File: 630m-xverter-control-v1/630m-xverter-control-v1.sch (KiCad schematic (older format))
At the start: 52 parts, among them J1 Rig Transverter, J2 ALC, J3 ANT, J4 TX_TO_AMP, J5 TX_FROM_AMP, J6 Power, J7 TX AMP POWER, K1 DS1E-M-DC12V, K2 DS1E-M-DC12V, K3 DS1E-M-DC12V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

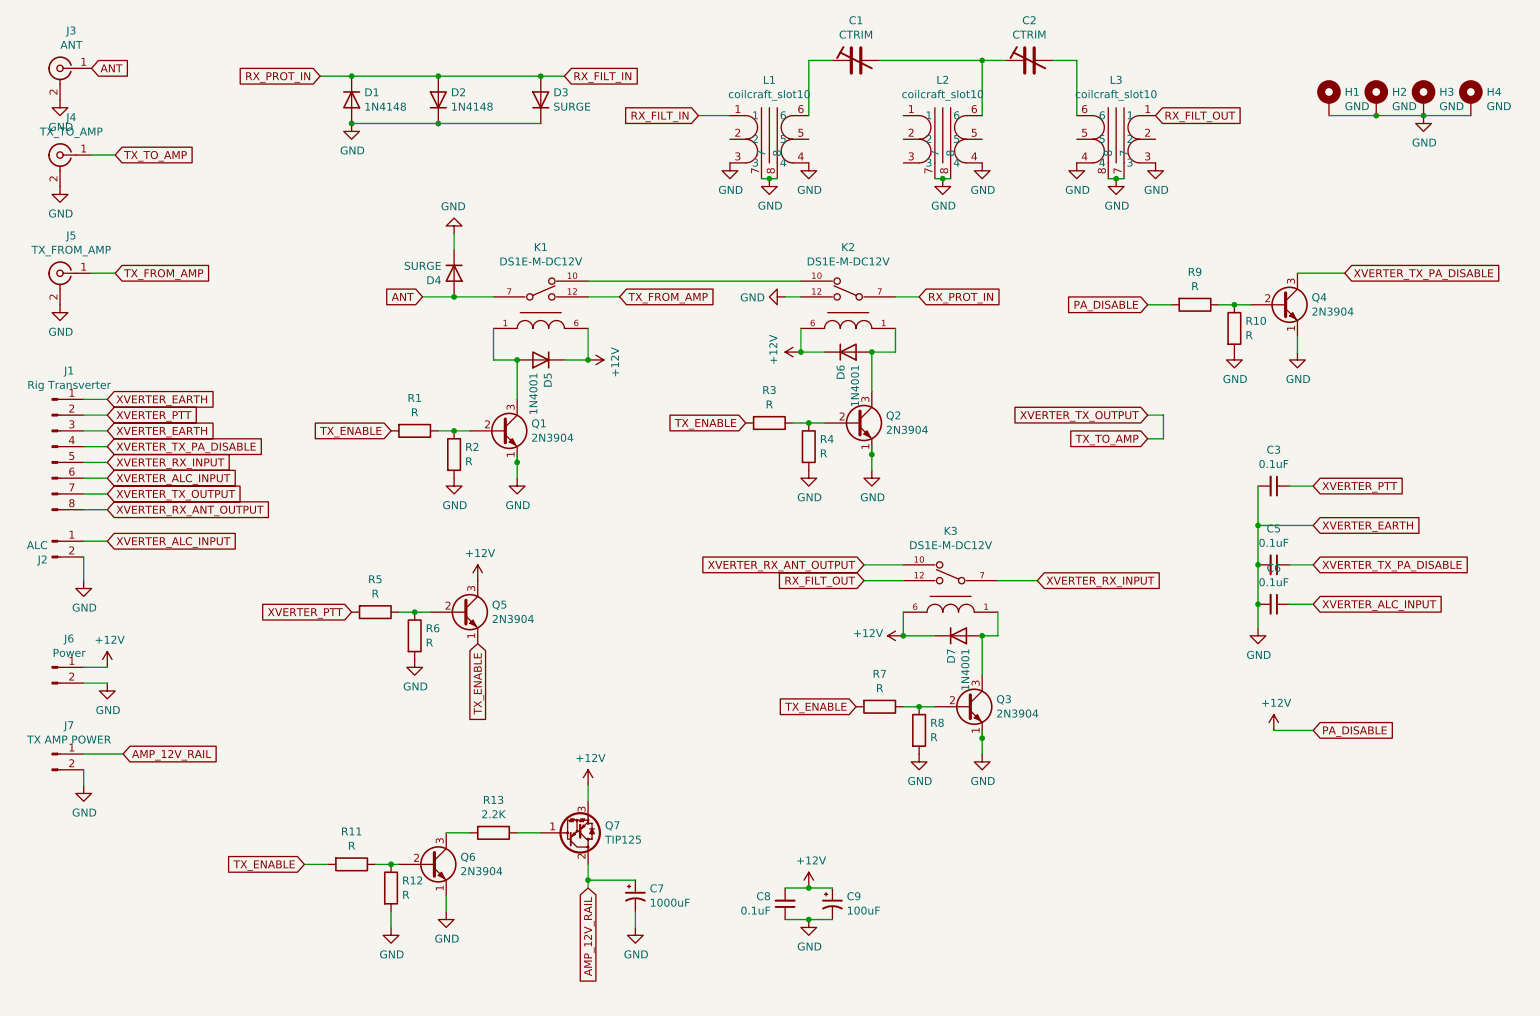
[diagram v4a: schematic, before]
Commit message: I got the fucking relay power backwards. WTAF.
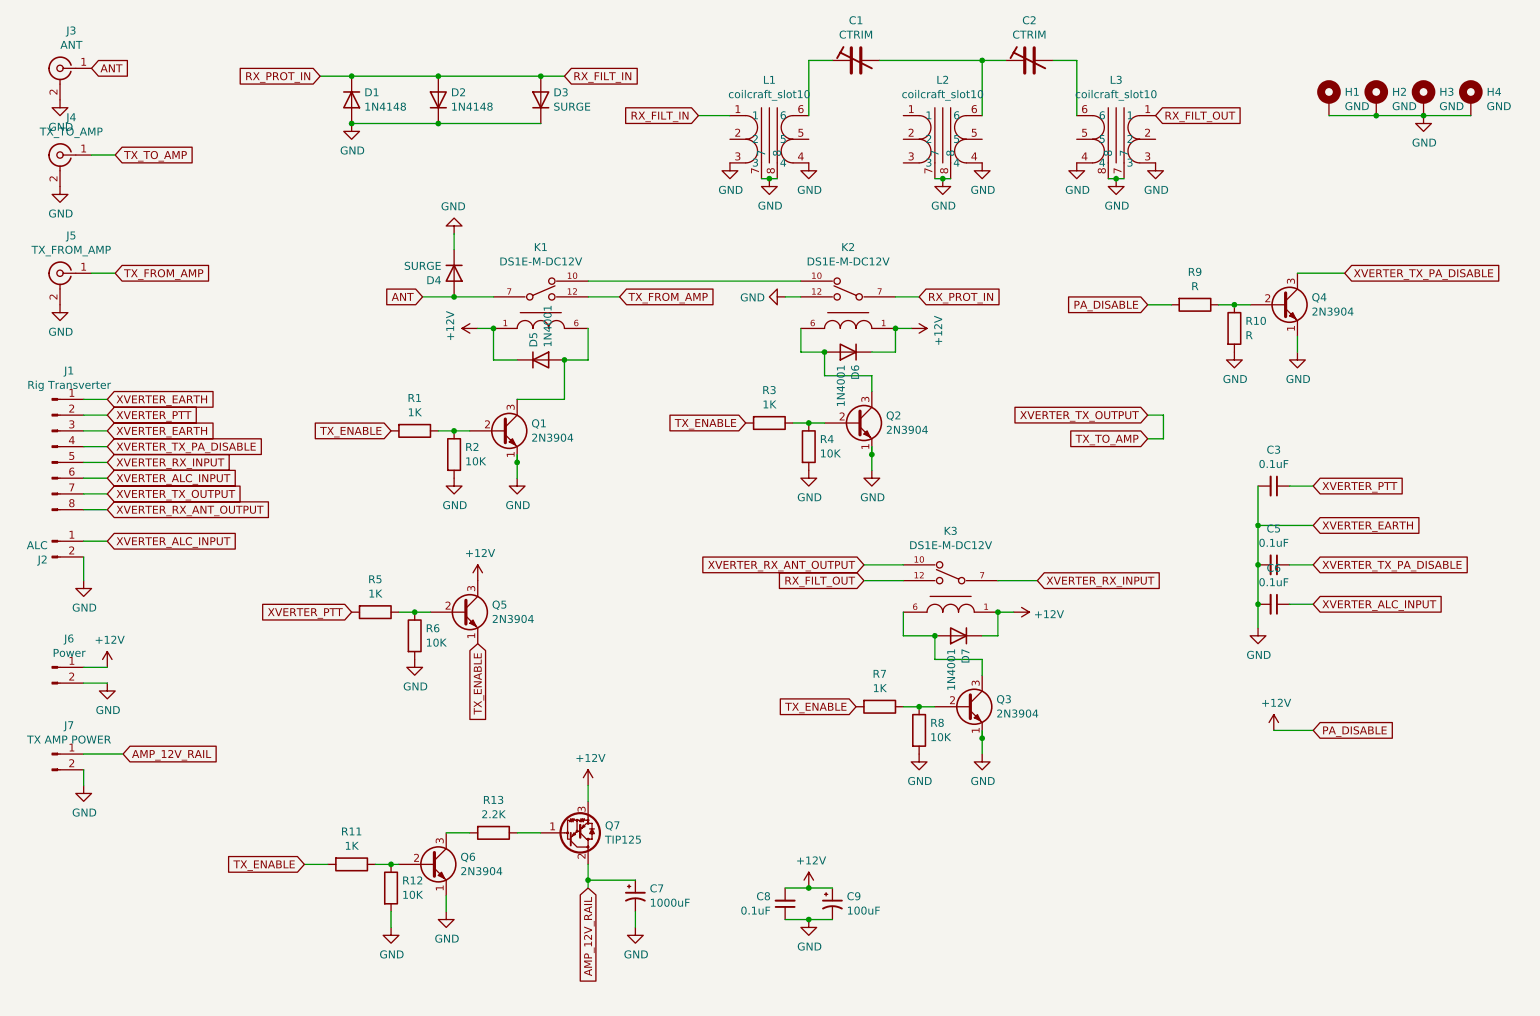
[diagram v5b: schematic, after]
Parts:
- C7: footprint Capacitor_THT:CP_Radial_D10.0mm_P2.50mm -> Capacitor_THT:CP_Radial_D10.0mm_P5.00mm
- R1, R11, R3, R5, R7: value R -> 1K
- R12, R2, R4, R6, R8: value R -> 10K
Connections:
- net +12V: now also K1.1, K2.1, K3.1; no longer K1.6, K2.6, K3.6
- net at D5.2 (A), Q1.3 (C): now also K1.6; no longer K1.1
- net at D6.2 (A), Q2.3 (C): now also K2.6; no longer K2.1
- net at D7.2 (A), Q3.3 (C): now also K3.6; no longer K3.1
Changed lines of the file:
@@
 P 3200 4300
 F 0 "R5" V 2993 4300 50  0000 C CNN
-F 1 "R" V 3084 4300 50  0000 C CNN
+F 1 "1K" V 3084 4300 50  0000 C CNN
 F 2 "Resistor_THT:R_Axial_DIN0207_L6.3mm_D2.5mm_P7.62mm_Horizontal" V 3130 4300 50  0001 C CNN
 F 3 "~" H 3200 4300 50  0001 C CNN
@@
 P 3450 4450
 F 0 "R6" H 3520 4496 50  0000 L CNN
-F 1 "R" H 3520 4405 50  0000 L CNN
+F 1 "10K" H 3520 4405 50  0000 L CNN
 F 2 "Resistor_THT:R_Axial_DIN0207_L6.3mm_D2.5mm_P7.62mm_Horizontal" V 3380 4450 50  0001 C CNN
 F 3 "~" H 3450 4450 50  0001 C CNN
@@
 F 3 "~" H 4250 2700 50  0001 C CNN
 	1    4250 2700
-	-1   0    0    1
+	1    0    0    -1
 $EndComp
 $Comp
@@
 F 3 "~" H 6200 2650 50  0001 C CNN
 	1    6200 2650
-	1    0    0    1
+	-1   0    0    1
 $EndComp
 $Comp
@@
 F 3 "~" H 6900 4450 50  0001 C CNN
 	1    6900 4450
-	1    0    0    1
+	-1   0    0    1
 $EndComp
 Text GLabel 9350 2150 2    50   Input ~ 0
@@
 P 3450 3150
 F 0 "R1" V 3243 3150 50  0000 C CNN
-F 1 "R" V 3334 3150 50  0000 C CNN
+F 1 "1K" V 3334 3150 50  0000 C CNN
 F 2 "Resistor_THT:R_Axial_DIN0207_L6.3mm_D2.5mm_P7.62mm_Horizontal" V 3380 3150 50  0001 C CNN
 F 3 "~" H 3450 3150 50  0001 C CNN
@@
 P 3700 3300
 F 0 "R2" H 3770 3346 50  0000 L CNN
-F 1 "R" H 3770 3255 50  0000 L CNN
+F 1 "10K" H 3770 3255 50  0000 L CNN
 F 2 "Resistor_THT:R_Axial_DIN0207_L6.3mm_D2.5mm_P7.62mm_Horizontal" V 3630 3300 50  0001 C CNN
 F 3 "~" H 3700 3300 50  0001 C CNN
@@
 L power:+12V #PWR0115
 U 1 1 5FC11DB6
-P 4550 2700
-F 0 "#PWR0115" H 4550 2550 50  0001 C CNN
-F 1 "+12V" H 4565 2873 50  0000 C CNN
-F 2 "" H 4550 2700 50  0001 C CNN
-F 3 "" H 4550 2700 50  0001 C CNN
-	1    4550 2700
-	0    1    1    0
+P 3850 2500
+F 0 "#PWR0115" H 3850 2350 50  0001 C CNN
+F 1 "+12V" H 3865 2673 50  0000 C CNN
+F 2 "" H 3850 2500 50  0001 C CNN
+F 3 "" H 3850 2500 50  0001 C CNN
+	1    3850 2500
+	0    -1   -1   0
 $EndComp
 $Comp
@@
 P 5700 3100
 F 0 "R3" V 5493 3100 50  0000 C CNN
-F 1 "R" V 5584 3100 50  0000 C CNN
+F 1 "1K" V 5584 3100 50  0000 C CNN
 F 2 "Resistor_THT:R_Axial_DIN0207_L6.3mm_D2.5mm_P7.62mm_Horizontal" V 5630 3100 50  0001 C CNN
 F 3 "~" H 5700 3100 50  0001 C CNN
@@
 P 5950 3250
 F 0 "R4" H 6020 3296 50  0000 L CNN
-F 1 "R" H 6020 3205 50  0000 L CNN
+F 1 "10K" H 6020 3205 50  0000 L CNN
 F 2 "Resistor_THT:R_Axial_DIN0207_L6.3mm_D2.5mm_P7.62mm_Horizontal" V 5880 3250 50  0001 C CNN
 F 3 "~" H 5950 3250 50  0001 C CNN
@@
 Wire Wire Line
 	6350 3300 6350 3400
-Wire Wire Line
-	6500 2500 6500 2650
-Wire Wire Line
-	6500 2650 6350 2650
-Wire Wire Line
-	6350 2900 6350 2650
-Connection ~ 6350 2650
-Wire Wire Line
-	4550 2500 4550 2700
-Wire Wire Line
-	4400 2700 4550 2700
-Connection ~ 4550 2700
-Wire Wire Line
-	3950 2500 3950 2700
-Wire Wire Line
-	3950 2700 4100 2700
-Wire Wire Line
-	4100 2700 4100 2950
-Connection ~ 4100 2700
 $Comp
 L power:+12V #PWR0119
 U 1 1 5FC3CB6F
-P 5900 2650
-F 0 "#PWR0119" H 5900 2500 50  0001 C CNN
-F 1 "+12V" H 5915 2823 50  0000 C CNN
-F 2 "" H 5900 2650 50  0001 C CNN
-F 3 "" H 5900 2650 50  0001 C CNN
-	1    5900 2650
-	0    -1   -1   0
-$EndComp
-Wire Wire Line
-	5900 2650 6050 2650
-Wire Wire Line
-	5900 2500 5900 2650
-Connection ~ 5900 2650
+P 6600 2500
+F 0 "#PWR0119" H 6600 2350 50  0001 C CNN
+F 1 "+12V" H 6615 2673 50  0000 C CNN
+F 2 "" H 6600 2500 50  0001 C CNN
+F 3 "" H 6600 2500 50  0001 C CNN
+	1    6600 2500
+	0    1    1    0
+$EndComp
 $Comp
 L Transistor_BJT:2N3904 Q3
@@
 P 6400 4900
 F 0 "R7" V 6193 4900 50  0000 C CNN
-F 1 "R" V 6284 4900 50  0000 C CNN
+F 1 "1K" V 6284 4900 50  0000 C CNN
 F 2 "Resistor_THT:R_Axial_DIN0207_L6.3mm_D2.5mm_P7.62mm_Horizontal" V 6330 4900 50  0001 C CNN
 F 3 "~" H 6400 4900 50  0001 C CNN
@@
 P 6650 5050
 F 0 "R8" H 6720 5096 50  0000 L CNN
-F 1 "R" H 6720 5005 50  0000 L CNN
+F 1 "10K" H 6720 5005 50  0000 L CNN
 F 2 "Resistor_THT:R_Axial_DIN0207_L6.3mm_D2.5mm_P7.62mm_Horizontal" V 6580 5050 50  0001 C CNN
 F 3 "~" H 6650 5050 50  0001 C CNN
@@
 Wire Wire Line
 	7050 5100 7050 5200
-Wire Wire Line
-	7050 4450 7050 4700
-Wire Wire Line
-	6550 4300 6550 4450
-Wire Wire Line
-	6550 4450 6750 4450
-Wire Wire Line
-	7150 4300 7150 4450
-Wire Wire Line
-	7150 4450 7050 4450
-Connection ~ 7050 4450
 $Comp
 L power:+12V #PWR0122
 U 1 1 5FC5222E
-P 6550 4450
-F 0 "#PWR0122" H 6550 4300 50  0001 C CNN
-F 1 "+12V" V 6565 4578 50  0000 L CNN
-F 2 "" H 6550 4450 50  0001 C CNN
-F 3 "" H 6550 4450 50  0001 C CNN
-	1    6550 4450
-	0    -1   -1   0
-$EndComp
-Connection ~ 6550 4450
+P 7250 4300
+F 0 "#PWR0122" H 7250 4150 50  0001 C CNN
+F 1 "+12V" V 7265 4428 50  0000 L CNN
+F 2 "" H 7250 4300 50  0001 C CNN
+F 3 "" H 7250 4300 50  0001 C CNN
+	1    7250 4300
+	0    1    1    0
+$EndComp
 Text GLabel 6250 4900 0    50   Input ~ 0
 TX_ENABLE
@@
 P 3050 5900
 F 0 "R11" V 2843 5900 50  0000 C CNN
-F 1 "R" V 2934 5900 50  0000 C CNN
+F 1 "1K" V 2934 5900 50  0000 C CNN
 F 2 "Resistor_THT:R_Axial_DIN0207_L6.3mm_D2.5mm_P7.62mm_Horizontal" V 2980 5900 50  0001 C CNN
 F 3 "~" H 3050 5900 50  0001 C CNN
@@
 P 3300 6050
 F 0 "R12" H 3370 6096 50  0000 L CNN
-F 1 "R" H 3370 6005 50  0000 L CNN
+F 1 "10K" H 3370 6005 50  0000 L CNN
 F 2 "Resistor_THT:R_Axial_DIN0207_L6.3mm_D2.5mm_P7.62mm_Horizontal" V 3230 6050 50  0001 C CNN
 F 3 "~" H 3300 6050 50  0001 C CNN
@@
 F 0 "C7" H 4941 6146 50  0000 L CNN
 F 1 "1000uF" H 4941 6055 50  0000 L CNN
-F 2 "Capacitor_THT:CP_Radial_D10.0mm_P2.50mm" H 4850 6100 50  0001 C CNN
+F 2 "Capacitor_THT:CP_Radial_D10.0mm_P5.00mm" H 4850 6100 50  0001 C CNN
 F 3 "~" H 4850 6100 50  0001 C CNN
 	1    4850 6100
@@
 Wire Wire Line
 	8800 3750 8800 4000
+Wire Wire Line
+	3950 2500 3850 2500
+Wire Wire Line
+	3950 2500 3950 2700
+Wire Wire Line
+	3950 2700 4100 2700
+Connection ~ 3950 2500
+Wire Wire Line
+	4550 2500 4550 2700
+Wire Wire Line
+	4550 2700 4400 2700
+Wire Wire Line
+	4400 2700 4400 2950
+Wire Wire Line
+	4400 2950 4100 2950
+Connection ~ 4400 2700
+Wire Wire Line
+	7150 4300 7250 4300
+Wire Wire Line
+	7150 4300 7150 4450
+Wire Wire Line
+	7150 4450 7050 4450
+Connection ~ 7150 4300
+Wire Wire Line
+	6550 4300 6550 4450
+Wire Wire Line
+	6550 4450 6750 4450
+Wire Wire Line
+	6750 4450 6750 4600
+Wire Wire Line
+	6750 4600 7050 4600
+Wire Wire Line
+	7050 4600 7050 4700
+Connection ~ 6750 4450
+Wire Wire Line
+	6500 2500 6600 2500
+Wire Wire Line
+	6500 2500 6500 2650
+Wire Wire Line
+	6500 2650 6350 2650
+Connection ~ 6500 2500
+Wire Wire Line
+	5900 2500 5900 2650
+Wire Wire Line
+	5900 2650 6050 2650
+Wire Wire Line
+	6350 2900 6350 2800
+Wire Wire Line
+	6350 2800 6050 2800
+Wire Wire Line
+	6050 2800 6050 2650
+Connection ~ 6050 2650
 $EndSCHEMATC
